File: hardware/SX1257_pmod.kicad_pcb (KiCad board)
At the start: 2 copper layers, 3 parts, among them J1 Conn_02x06_Odd_Even, U1 SX1257, Y1 32/36MHz ?ppm

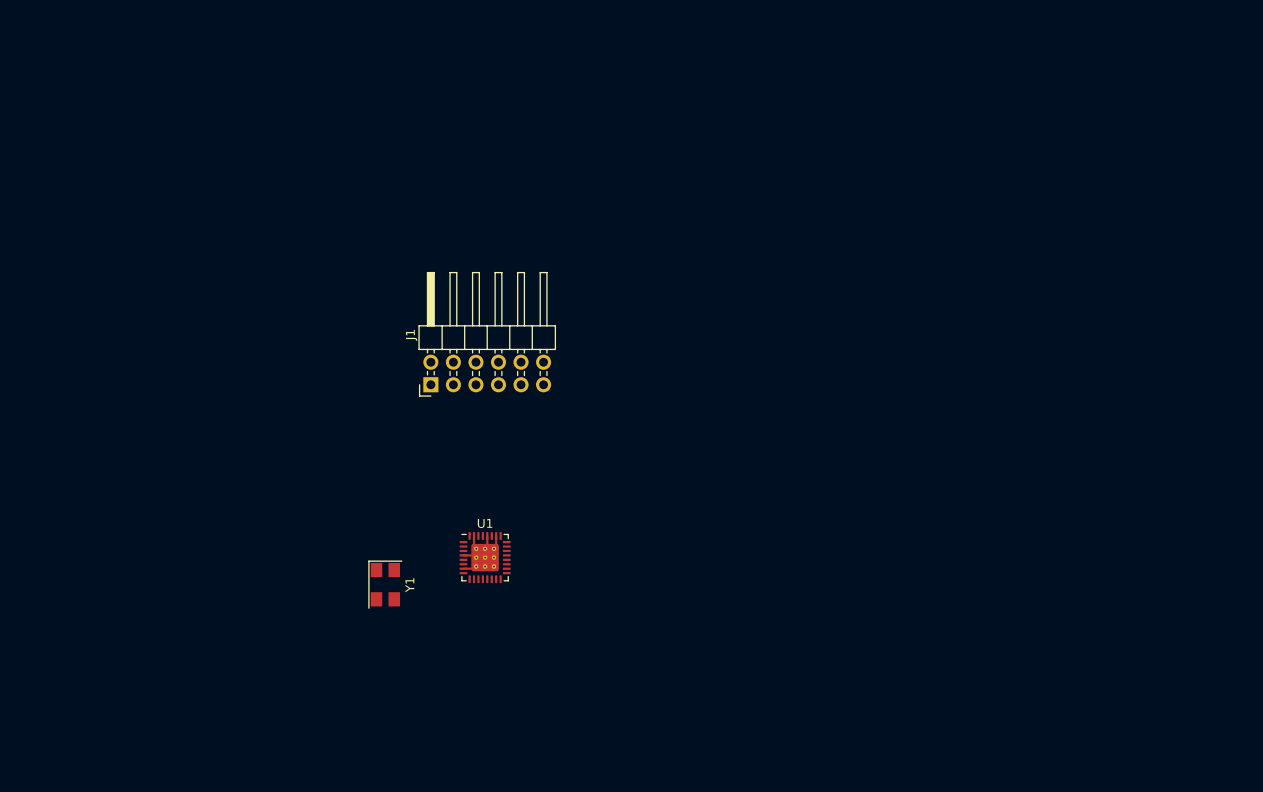
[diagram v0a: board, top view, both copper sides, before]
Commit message: Initial PCB routing
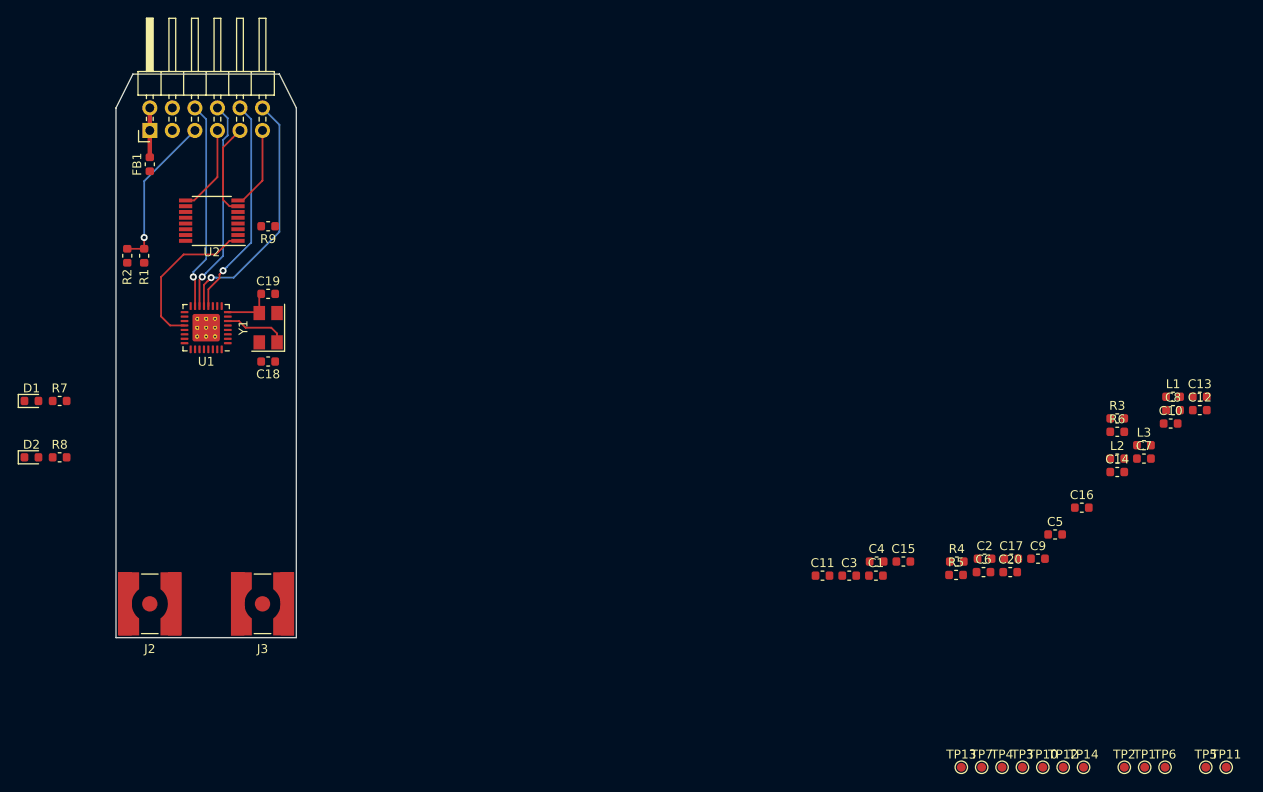
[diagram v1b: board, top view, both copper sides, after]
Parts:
- added C1: 2.7p, Capacitor_SMD:C_0603_1608Metric, F.Cu at (199.9, 79.4)
- added C10: 100n, Capacitor_SMD:C_0603_1608Metric, F.Cu at (233.1, 62.2)
- added C11: 100n, Capacitor_SMD:C_0603_1608Metric, F.Cu at (193.9, 79.4)
- added C12: 10n, Capacitor_SMD:C_0603_1608Metric, F.Cu at (236.4, 60.7)
- added C13: 10n, Capacitor_SMD:C_0603_1608Metric, F.Cu at (236.4, 59.2)
- added C14: 1u, Capacitor_SMD:C_0603_1608Metric, F.Cu at (227.1, 67.7)
- added C15: 1u, Capacitor_SMD:C_0603_1608Metric, F.Cu at (203.0, 77.8)
- added C16: 1u, Capacitor_SMD:C_0603_1608Metric, F.Cu at (223.1, 71.7)
- added C17: 10u, Capacitor_SMD:C_0603_1608Metric, F.Cu at (215.2, 77.5)
- added C18: 16p, Capacitor_SMD:C_0603_1608Metric, F.Cu at (131.4, 55.2)
- added C19: 16p, Capacitor_SMD:C_0603_1608Metric, F.Cu at (131.4, 47.6)
- added C2: 3.3p, Capacitor_SMD:C_0603_1608Metric, F.Cu at (212.2, 77.5)
- added C20: 100n, Capacitor_SMD:C_0603_1608Metric, F.Cu at (215.1, 79.0)
- added C3: 33p, Capacitor_SMD:C_0603_1608Metric, F.Cu at (196.9, 79.4)
- added C4: 10p, Capacitor_SMD:C_0603_1608Metric, F.Cu at (200.0, 77.8)
- added C5: 3.3p, Capacitor_SMD:C_0603_1608Metric, F.Cu at (220.1, 74.7)
- added C6: 100n, Capacitor_SMD:C_0603_1608Metric, F.Cu at (212.1, 79.0)
- added C7: 5.6p, Capacitor_SMD:C_0603_1608Metric, F.Cu at (230.1, 66.2)
- added C8: 10p, Capacitor_SMD:C_0603_1608Metric, F.Cu at (233.4, 60.7)
- added C9: 100n, Capacitor_SMD:C_0603_1608Metric, F.Cu at (218.2, 77.5)
- added D1: LED, LED_SMD:LED_0603_1608Metric, F.Cu at (104.8, 59.7)
- added D2: LED, LED_SMD:LED_0603_1608Metric, F.Cu at (104.8, 66.0)
- added FB1: Ferrite_Bead, Inductor_SMD:L_0603_1608Metric, F.Cu at (118.1, 33.0)
- added J2: SMA_F_RX, Connector_Coaxial:SMA_Amphenol_132134-10_Vertical, F.Cu at (118.1, 82.5)
- added J3: SMA_F_TX, Connector_Coaxial:SMA_Amphenol_132134-10_Vertical, F.Cu at (130.8, 82.5)
- added L1: 15nH, Inductor_SMD:L_0603_1608Metric, F.Cu at (233.4, 59.2)
- added L2: 10n, Inductor_SMD:L_0603_1608Metric, F.Cu at (227.1, 66.2)
- added L3: 12n, Inductor_SMD:L_0603_1608Metric, F.Cu at (230.1, 64.7)
- added R1: 0R, Resistor_SMD:R_0603_1608Metric, F.Cu at (117.5, 43.3)
- added R2: 0R, Resistor_SMD:R_0603_1608Metric, F.Cu at (115.6, 43.3)
- added R3: 0R, Resistor_SMD:R_0603_1608Metric, F.Cu at (227.1, 61.7)
- added R4: 0R, Resistor_SMD:R_0603_1608Metric, F.Cu at (209.0, 77.8)
- added R5: 0R, Resistor_SMD:R_0603_1608Metric, F.Cu at (209.0, 79.3)
- added R6: 0R, Resistor_SMD:R_0603_1608Metric, F.Cu at (227.1, 63.2)
- added R7: 2k, Resistor_SMD:R_0603_1608Metric, F.Cu at (108.0, 59.7)
- added R8: 2k, Resistor_SMD:R_0603_1608Metric, F.Cu at (108.0, 66.0)
- added R9: 10k, Resistor_SMD:R_0603_1608Metric, F.Cu at (131.4, 40.0)
- added TP1: TestPoint, TestPoint:TestPoint_Pad_D1.0mm, F.Cu at (230.2, 101.0)
- added TP10: TestPoint, TestPoint:TestPoint_Pad_D1.0mm, F.Cu at (218.7, 101.0)
- added TP11: TestPoint, TestPoint:TestPoint_Pad_D1.0mm, F.Cu at (239.4, 101.0)
- added TP12: TestPoint, TestPoint:TestPoint_Pad_D1.0mm, F.Cu at (221.0, 101.0)
- added TP13: TestPoint, TestPoint:TestPoint_Pad_D1.0mm, F.Cu at (209.6, 101.0)
- added TP14: TestPoint, TestPoint:TestPoint_Pad_D1.0mm, F.Cu at (223.3, 101.0)
- added TP2: TestPoint, TestPoint:TestPoint_Pad_D1.0mm, F.Cu at (227.9, 101.0)
- added TP3: TestPoint, TestPoint:TestPoint_Pad_D1.0mm, F.Cu at (216.4, 101.0)
- added TP4: TestPoint, TestPoint:TestPoint_Pad_D1.0mm, F.Cu at (214.1, 101.0)
- added TP5: TestPoint, TestPoint:TestPoint_Pad_D1.0mm, F.Cu at (237.1, 101.0)
- added TP6: TestPoint, TestPoint:TestPoint_Pad_D1.0mm, F.Cu at (232.5, 101.0)
- added TP7: TestPoint, TestPoint:TestPoint_Pad_D1.0mm, F.Cu at (211.8, 101.0)
- added U2: SC18IS602B, Package_SO:TSSOP-16_4.4x5mm_P0.65mm, F.Cu at (125.1, 39.4)
- moved J1 42.7 mm to (118.1, 29.2)
- moved U1 40.7 mm to (124.5, 51.4), turned to 180 degrees
- moved Y1 31.8 mm to (131.4, 51.4), turned to 90 degrees
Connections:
- J1 pad 1: +3V3 -> /PMOD_3V3
- J1 pad 11: /PMOD_1 -> /I2C_CLK
- J1 pad 2: +3V3 -> /PMOD_3V3
- J1 pad 7: /PMOD_3 -> /I2C_INT
- J1 pad 9: /PMOD_2 -> /I2C_SDA
- U1 pad 1: Net-(U1-Pad1) -> +3V3
- U1 pad 16: Net-(U1-Pad16) -> +3V3
- U1 pad 17: /PMOD_4 -> /SPI_SCK
- U1 pad 18: /PMOD_3 -> /SPI_MISO
- U1 pad 19: /PMOD_2 -> /SPI_MOSI
- U1 pad 2: Net-(U1-Pad2) -> +3V3
- U1 pad 20: /PMOD_1 -> /SPI_NSS
- U1 pad 21: Net-(U1-Pad21) -> /DIO0
- U1 pad 22: Net-(U1-Pad22) -> /DIO1
- U1 pad 23: Net-(U1-Pad23) -> /DIO2
- U1 pad 24: Net-(U1-Pad24) -> /DIO3
- U1 pad 25: Net-(U1-Pad25) -> +3V3
- U1 pad 27: Net-(U1-Pad27) -> /RF_IN
- U1 pad 29: Net-(U1-Pad29) -> /RF_ON
- U1 pad 3: Net-(U1-Pad3) -> +3V3
- U1 pad 30: Net-(U1-Pad30) -> /RF_OP
- U1 pad 32: Net-(U1-Pad32) -> +3V3
- U1 pad 5: Net-(U1-Pad5) -> +3V3
- U1 pad 9: Net-(U1-Pad9) -> /RESET
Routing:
- net /PMOD_5: track 0.00 -> 28.1 mm, vias 0 -> 1
- net /PMOD_6: track 0.00 -> 24.9 mm, vias 0 -> 1
- net /PMOD_7: track 0.00 -> 24.3 mm, vias 0 -> 1
- net /PMOD_8: track 0.00 -> 23.7 mm, vias 0 -> 1
- net /SPI_NSS: track 0.00 -> 17.9 mm
- net /PMOD_4: track 0.00 -> 17.6 mm, vias 0 -> 1
- net GND: track 11.9 -> 0.00 mm
- net /I2C_SDA: track 0.00 -> 10.6 mm
- net /I2C_INT: track 0.00 -> 9.93 mm
- net /I2C_CLK: track 0.00 -> 9.34 mm
- net /XTA: track 0.00 -> 7.13 mm
- net /XTB: track 0.00 -> 5.84 mm
- net /PMOD_3V3: track 0.00 -> 5.56 mm
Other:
- board outline added: 20.3 x 63.5 mm
- net class Default: clearance 0.2 -> 0.2032; trace_width 0.25 -> 0.2032
- rule trace_clearance: 0.2 -> 0.2032

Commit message: Some improvements and pcb work
- Connected gpio1 to SX_RESET
- Removed R0 for CLK select
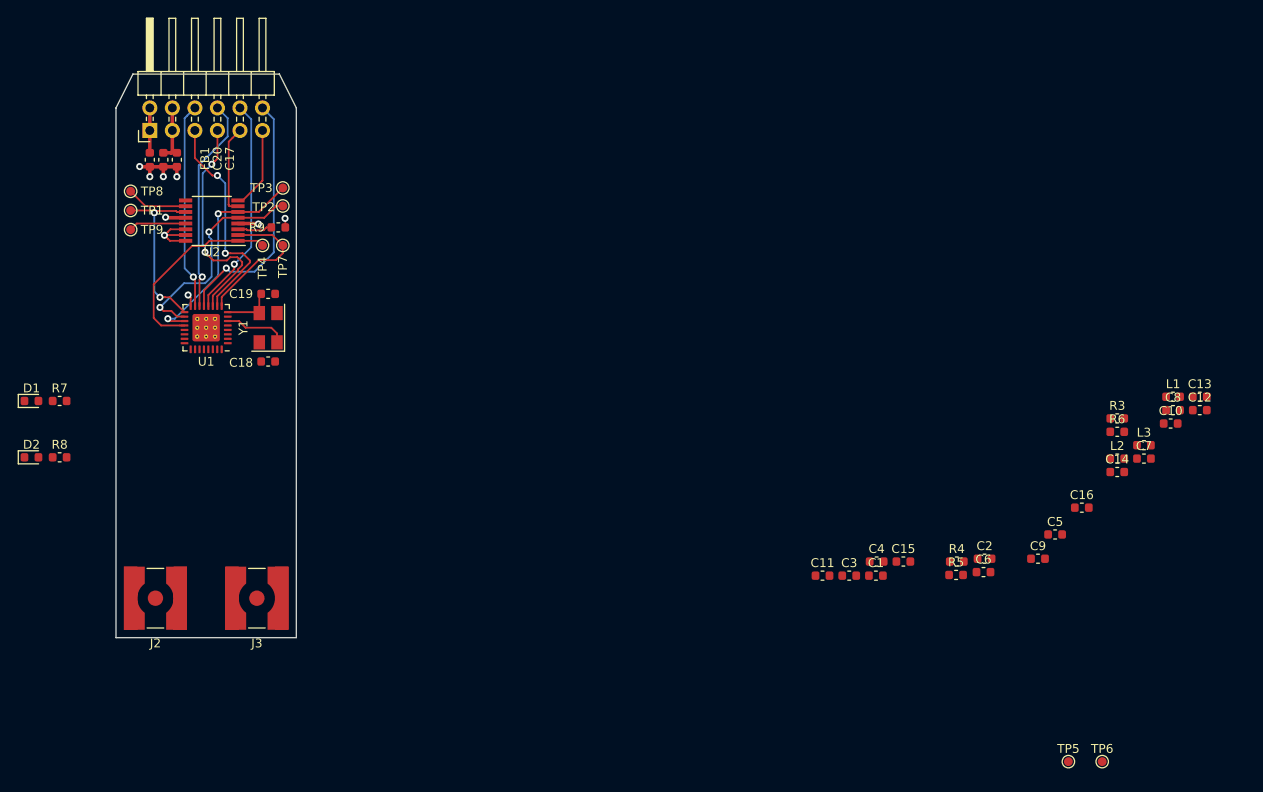
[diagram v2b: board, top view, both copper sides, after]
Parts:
- removed R1, R2: 0R, Resistor_SMD:R_0603_1608Metric
- removed TP10, TP11, TP12, TP13, TP14: TestPoint, TestPoint:TestPoint_Pad_D1.0mm
- added TP8: TestPoint, TestPoint:TestPoint_Pad_D1.0mm, F.Cu at (116.0, 36.1)
- added TP9: TestPoint, TestPoint:TestPoint_Pad_D1.0mm, F.Cu at (116.0, 40.4)
- moved TP1 130.4 mm to (116.0, 38.2), turned to 90 degrees
- moved TP2 114.0 mm to (133.1, 37.7), turned to 90 degrees
- moved TP3 105.9 mm to (133.1, 35.7), turned to 90 degrees
- moved C17 105.6 mm to (119.6, 32.5), turned to 90 degrees
- moved C20 104.8 mm to (121.2, 32.5), turned to 90 degrees
- moved TP4 102.0 mm to (130.8, 42.2), turned to 270 degrees
- moved TP7 98.3 mm to (133.1, 42.2), turned to 270 degrees
- moved TP5 15.5 mm to (221.6, 100.3)
- moved TP6 7.11 mm to (225.4, 100.3)
- moved R9 1.15 mm to (132.6, 40.1)
- moved J2 0.90 mm to (118.7, 81.9)
- moved J3 0.90 mm to (130.2, 81.9)
- moved FB1 0.51 mm to (118.1, 32.5)
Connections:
- J1 pad 5: /PMOD_4 -> /CLK_OUT
- J1 pad 7: /I2C_INT -> /CLK_IN
- TP1 pad 1: /RESET -> /SPI_SCK
- TP2 pad 1: /CLK_OUT -> /SPI_MISO
- TP3 pad 1: /CLK_IN -> /SPI_MOSI
- TP4 pad 1: /SPI_SCK -> /SPI_NSS
- TP5 pad 1: /SPI_MISO -> /DIO2
- TP6 pad 1: /SPI_MOSI -> /DIO3
- TP7 pad 1: /SPI_NSS -> /SX_RESET
- U1 pad 9: /RESET -> /SX_RESET
- U2 pad 2: /GPIO1 -> /SX_RESET
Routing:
- net /CLK_IN: track 0.00 -> 25.8 mm, vias 0 -> 2
- net /CLK_OUT: track 0.00 -> 25.4 mm, vias 0 -> 2
- net /SPI_MISO: track 0.00 -> 25.2 mm, vias 0 -> 2
- net /SPI_MOSI: track 0.00 -> 25.1 mm, vias 0 -> 2
- net /SPI_SCK: track 0.00 -> 19.7 mm, vias 0 -> 2
- net /PMOD_4: track 17.6 -> 0.00 mm, vias 1 -> 0
- net GND: track 0.00 -> 16.7 mm, vias 0 -> 2
- net /SX_RESET: track 0.00 -> 16.4 mm
- net +3V3: track 0.00 -> 12.2 mm, vias 0 -> 7
- net /I2C_INT: track 9.93 -> 0.00 mm
- net /GPIO2: track 0.00 -> 6.89 mm
- net /GPIO3: track 0.00 -> 6.48 mm
- net /SPI_NSS: track 17.9 -> 22.1 mm
- net Net-(R9-Pad2): track 0.00 -> 3.93 mm
- net /I2C_SDA: track 10.6 -> 10.1 mm
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- added copper zone on In2.Cu, net +3V3
- added copper zone on In1.Cu, net GND
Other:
- copper layers 2 -> 4

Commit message: PCB design almost done.
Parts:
- removed R3, R4, R5, R6: 0R, Resistor_SMD:R_0603_1608Metric
- J2, J3: footprint Connector_Coaxial:SMA_Amphenol_132134-10_Vertical -> extra:CON-SMA-EDGE
- Y1: value 32/36MHz ?ppm -> 36MHz 10ppm; footprint Crystal:Crystal_SMD_5032-4Pin_5.0x3.2mm -> Crystal:Crystal_SMD_3225-4Pin_3.2x2.5mm
- moved TP6 118.8 mm to (116.0, 54.1), turned to 90 degrees
- moved TP5 116.2 mm to (116.0, 51.9), turned to 90 degrees
- moved C12 115.8 mm to (121.4, 46.7), turned to 180 degrees
- moved C13 115.6 mm to (120.9, 55.4), turned to 180 degrees
- moved C7 114.6 mm to (115.7, 59.5), turned to 90 degrees
- moved L1 113.1 mm to (120.3, 58.0), turned to 270 degrees
- moved L3 113.0 mm to (117.2, 59.6), turned to 90 degrees
- moved C8 103.9 mm to (129.5, 59.6), turned to 90 degrees
- moved C16 102.9 mm to (128.0, 32.5), turned to 270 degrees
- moved C10 102.8 mm to (131.4, 47.0)
- moved C9 102.8 mm to (125.7, 32.5), turned to 270 degrees
- moved C14 102.3 mm to (131.1, 32.5), turned to 270 degrees
- moved L2 100.2 mm to (127.3, 57.3)
- moved C6 96.7 mm to (121.4, 45.2), turned to 180 degrees
- moved C5 91.5 mm to (130.3, 57.3)
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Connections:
- J2 pad 1: Net-(J2-Pad1) -> Net-(C4-Pad1)
- J3 pad 1: Net-(J3-Pad1) -> Net-(C8-Pad1)
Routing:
- net GND: track 16.7 -> 82.3 mm, vias 2 -> 41
- net +3V3: track 12.2 -> 37.9 mm, vias 7 -> 13
- net /DIO0: track 0.00 -> 11.1 mm
- net Net-(C4-Pad1): track 0.00 -> 8.45 mm
- net /DIO1: track 0.00 -> 7.24 mm
- net /RF_IN: track 0.00 -> 7.07 mm
- net /DIO3: track 0.00 -> 6.45 mm
- net /DIO2: track 0.00 -> 6.38 mm
- net /RF_OP: track 0.00 -> 5.58 mm
- net Net-(C8-Pad1): track 0.00 -> 5.47 mm
- net /RF_ON: track 0.00 -> 5.13 mm
- net Net-(C5-Pad1): track 0.00 -> 2.96 mm
- net /I2C_CLK: track 9.34 -> 11.2 mm
- net Net-(D1-Pad2): track 0.00 -> 1.65 mm
- net Net-(D2-Pad2): track 0.00 -> 1.65 mm
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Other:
- board size 20.3 x 63.5 mm -> 20.3 x 45.5 mm

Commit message: Final touches of the pcb
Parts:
- moved U2 0.64 mm to (124.5, 39.4)
- moved C9 0.25 mm to (125.5, 32.5)
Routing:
- net +3V3: track 37.9 -> 38.9 mm, vias 13 -> 14
- net /I2C_SDA: track 10.3 -> 11.2 mm
- net /SPI_SCK: track 19.8 -> 20.3 mm
- net GND: track 82.3 -> 82.5 mm, vias 41 -> 42
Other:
- net class Default: clearance 0.2032 -> 0.1524; trace_width 0.2032 -> 0.1524
- rule trace_clearance: 0.2032 -> 0.1524
- rule trace_min: 0.2 -> 0.1524
- board text added: "RX"
- board text added: "TX"

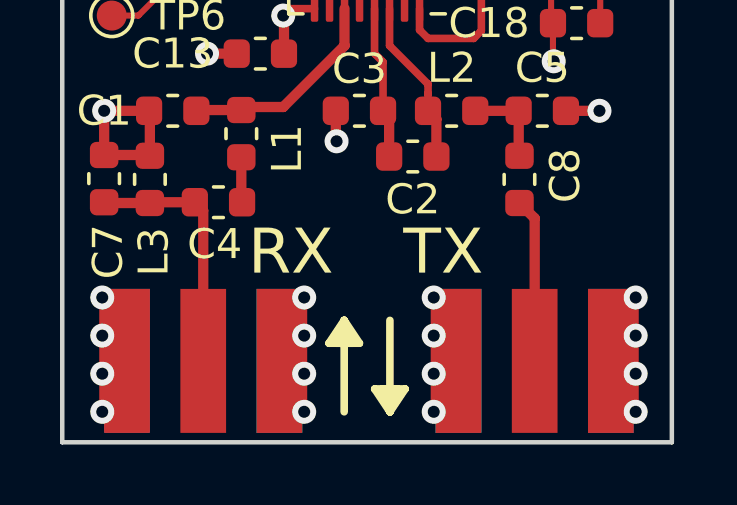
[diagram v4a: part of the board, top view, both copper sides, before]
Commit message: RevA: Minor changes and produce gerbers
- Moved the SMA connectors closed to the edges
- Added silk on the back
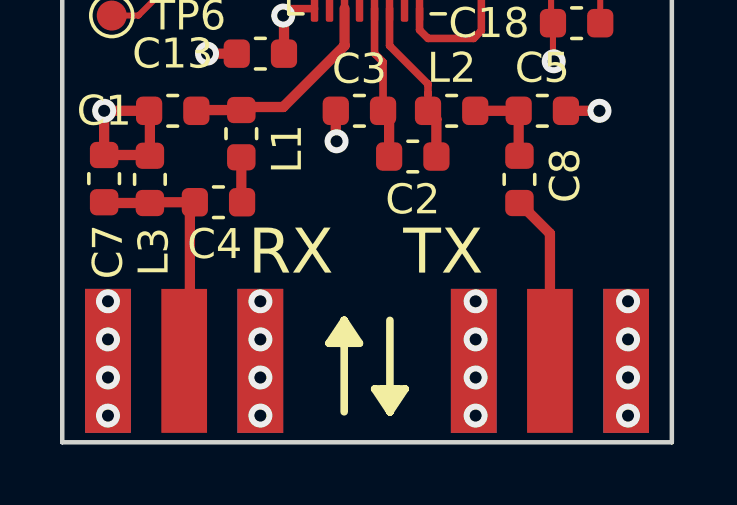
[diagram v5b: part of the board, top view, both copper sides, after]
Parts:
- added LOGO1: Logo_Open_Hardware_Large, extra:oshw_logo, B.Cu at (122.1, 57.1)
- moved J2 0.63 mm to (118.4, 65.9)
- moved J3 0.51 mm to (130.6, 65.9)
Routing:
- net GND: track 82.5 -> 75.4 mm
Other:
- board text added: "SX1257 PMOD 2019-01 RevA @kbeckmann @ico_TC @tnt"
